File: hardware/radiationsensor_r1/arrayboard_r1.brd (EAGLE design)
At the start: 22 parts, among them CN0 RADIATION-SENSOR-REV1, CN1 RADIATION-SENSOR-REV1, CN10 RADIATION-SENSOR-REV1, CN11 RADIATION-SENSOR-REV1, CN12 RADIATION-SENSOR-REV1, CN13 RADIATION-SENSOR-REV1, CN14 RADIATION-SENSOR-REV1, CN15 RADIATION-SENSOR-REV1, CN16 2524-, CN17 22-23-2041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

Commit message: partial routing for imaging array rev1
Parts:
- moved U1 2.60 mm to (36.3, 74.7), turned to 90 degrees
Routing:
- net CS15: track 0.00 -> 106.1 mm
- net CS14: track 0.00 -> 100.8 mm
- net CS13: track 0.00 -> 98.0 mm
- net VBIAS: track 0.00 -> 97.1 mm
- net 5V: track 0.00 -> 94.8 mm
- net GND: track 0.00 -> 92.5 mm
- net CS12: track 0.00 -> 86.1 mm
- net MOSI: track 0.00 -> 85.8 mm
- net CS11: track 0.00 -> 84.0 mm
- net SCLK: track 0.00 -> 83.5 mm
- net CS10: track 0.00 -> 72.1 mm
- net CS9: track 0.00 -> 69.9 mm
- net CS7: track 0.00 -> 69.2 mm
- net CS8: track 0.00 -> 58.7 mm
- net CS6: track 0.00 -> 57.4 mm
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
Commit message: additional routing
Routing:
- net VTEMP4: track 0.00 -> 122.5 mm, vias 0 -> 1
- net VTEMP11: track 0.00 -> 89.1 mm, vias 0 -> 1
- net COMP15: track 0.00 -> 65.0 mm
- net COMP14: track 0.00 -> 59.2 mm
- net COMP13: track 0.00 -> 53.3 mm
- net COMP1: track 0.00 -> 52.4 mm
- net COMP12: track 0.00 -> 49.8 mm
- net COMP0: track 0.00 -> 48.1 mm
- net COMP11: track 0.00 -> 43.2 mm
- net COMP3: track 0.00 -> 42.0 mm
- net COMP10: track 0.00 -> 39.9 mm
- net COMP2: track 0.00 -> 38.1 mm
- net COMP9: track 0.00 -> 33.1 mm
- net COMP5: track 0.00 -> 31.1 mm
- net COMP8: track 0.00 -> 29.5 mm
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
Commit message: additional routing
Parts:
- moved C1 11.9 mm to (46.0, 77.4)
- moved R1 10.5 mm to (44.0, 77.4)
- moved CN16 0.50 mm to (75.3, 81.1)
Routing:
- net VLOGIC: track 0.00 -> 59.2 mm
- net SDA: track 0.00 -> 47.5 mm
- net SCL: track 0.00 -> 46.3 mm
- net N$2: track 0.00 -> 14.4 mm, vias 0 -> 2
- net VTEMP11: track 89.1 -> 89.6 mm
- net COMP9: track 33.1 -> 33.6 mm
- net COMP15: track 65.0 -> 65.5 mm
- net COMP13: track 53.3 -> 53.8 mm
- net COMP1: track 52.4 -> 52.9 mm

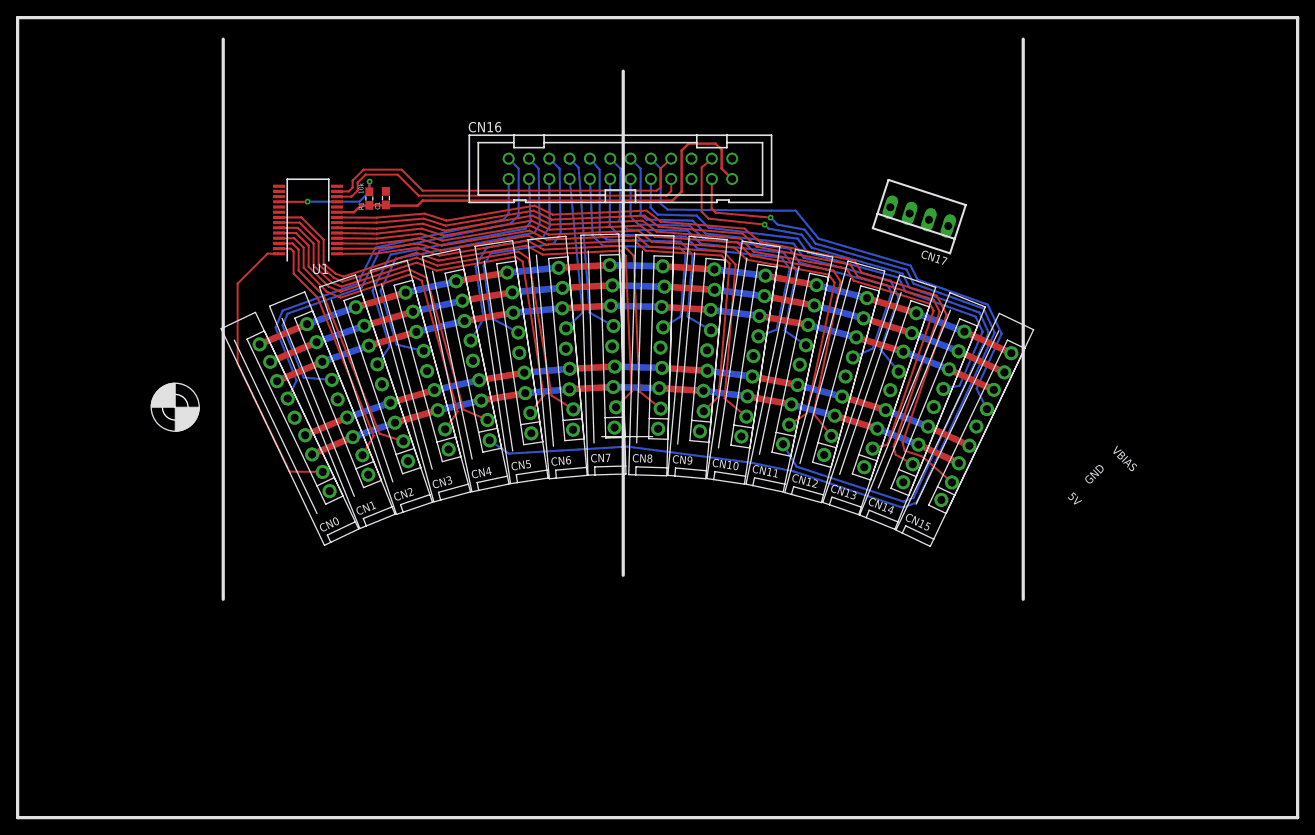
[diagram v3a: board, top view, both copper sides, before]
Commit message: finished routing for imaging array board rev1
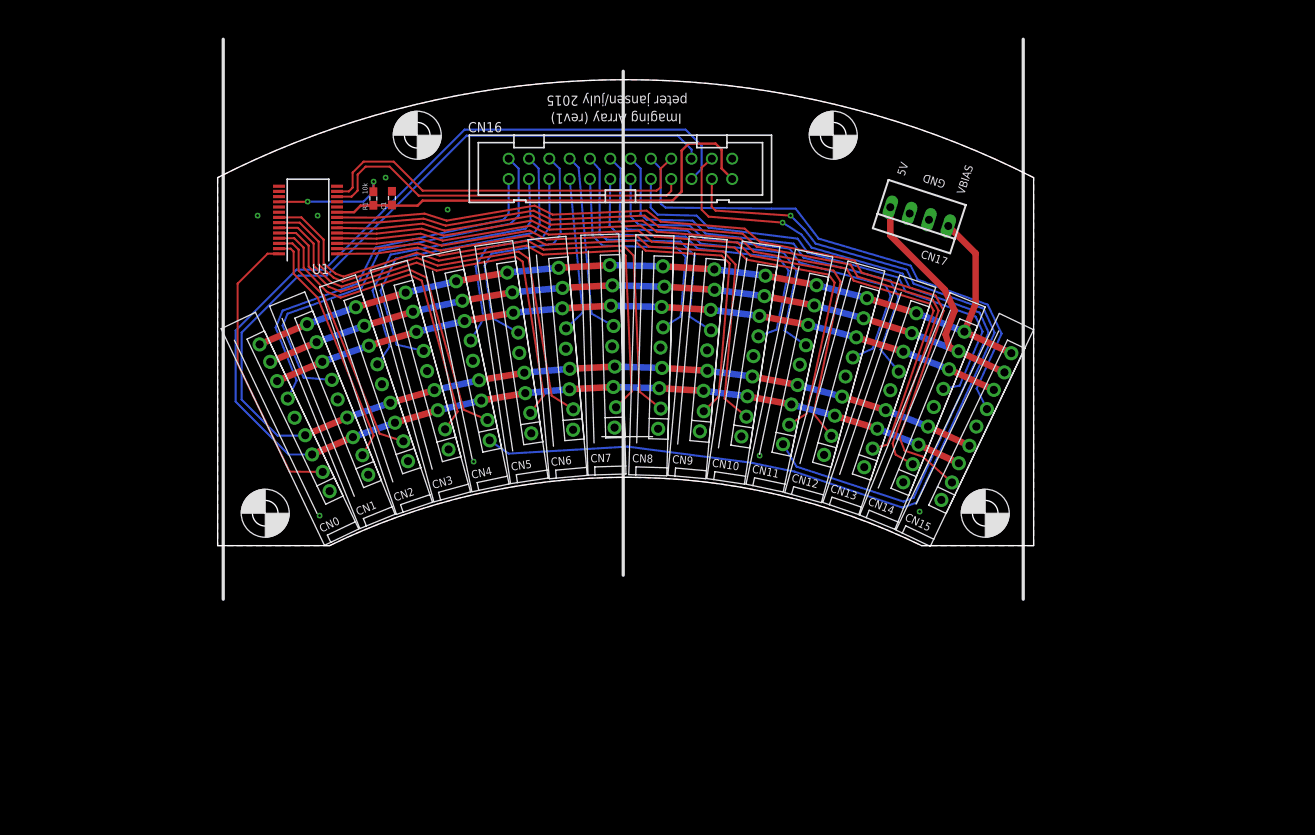
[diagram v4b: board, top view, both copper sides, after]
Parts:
- added U$35, U$36, U$37: (no value), openct:MOUNT-M3
- moved U$38 45.5 mm to (50.0, 85.3)
- moved C1 0.75 mm to (46.8, 77.4)
- moved R1 0.50 mm to (44.5, 77.4)
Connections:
- net 5V: now also CN17.4; no longer CN17.1
- net VBIAS: now also CN17.1; no longer CN17.4
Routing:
- net SCLK: track 83.5 -> 178.8 mm
- net MOSI: track 85.8 -> 172.3 mm
- net 5V: track 94.8 -> 116.9 mm
- net VBIAS: track 97.1 -> 111.9 mm
- net SDA: track 47.5 -> 48.9 mm
- net SCL: track 46.3 -> 47.7 mm
- net VLOGIC: track 59.2 -> 60.5 mm
- net N$2: track 14.4 -> 14.9 mm
- net GND: vias 0 -> 8
- added copper zone on layer 1, net GND
- added copper zone on layer 16, net GND
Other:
- board outline added: 102 x 58.2 mm
- board text added: "Imaging Array (rev1)"
- board text added: "peter jansen/july 2015"
